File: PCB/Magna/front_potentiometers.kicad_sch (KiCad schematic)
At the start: 24 parts

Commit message: Add final touched to all schematics
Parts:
- removed RV23: 10k, symbol Device:R_Potentiometer_Small
- added RV1421: 10k, symbol Device:R_Potentiometer_Small
- renumbered RV19 to RV1401, RV21 to RV1402, RV24 to RV1403, RV20 to RV1404, RV22 to RV1405, RV18 to RV1406, RV2 to RV1407, RV7 to RV1408, RV11 to RV1409, RV1 to RV1410, RV6 to RV1411, RV10 to RV1412, RV14 to RV1413, RV16 to RV1414, RV13 to RV1415, RV15 to RV1416, RV17 to RV1417, RV9 to RV1418, RV5 to RV1419, RV8 to RV1420, RV3 to RV1422, RV4 to RV1423, RV12 to RV1424
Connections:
- net SPARE7 is gone; now on net SPARE1: RV1403.2
- net GND: now also RV1421.3
- net SPARE1: no longer RV1406.2
- net VDDA: now also RV1421.1
- new net CH1_GAIN: RV1406.2
- new net CH2_GAIN: RV1421.2
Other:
- note added: "GAIN"
- note added: "Spare potentiometers"
- moved on the sheet: RV1401, RV1402, RV1403, RV1404, RV1405, RV1406

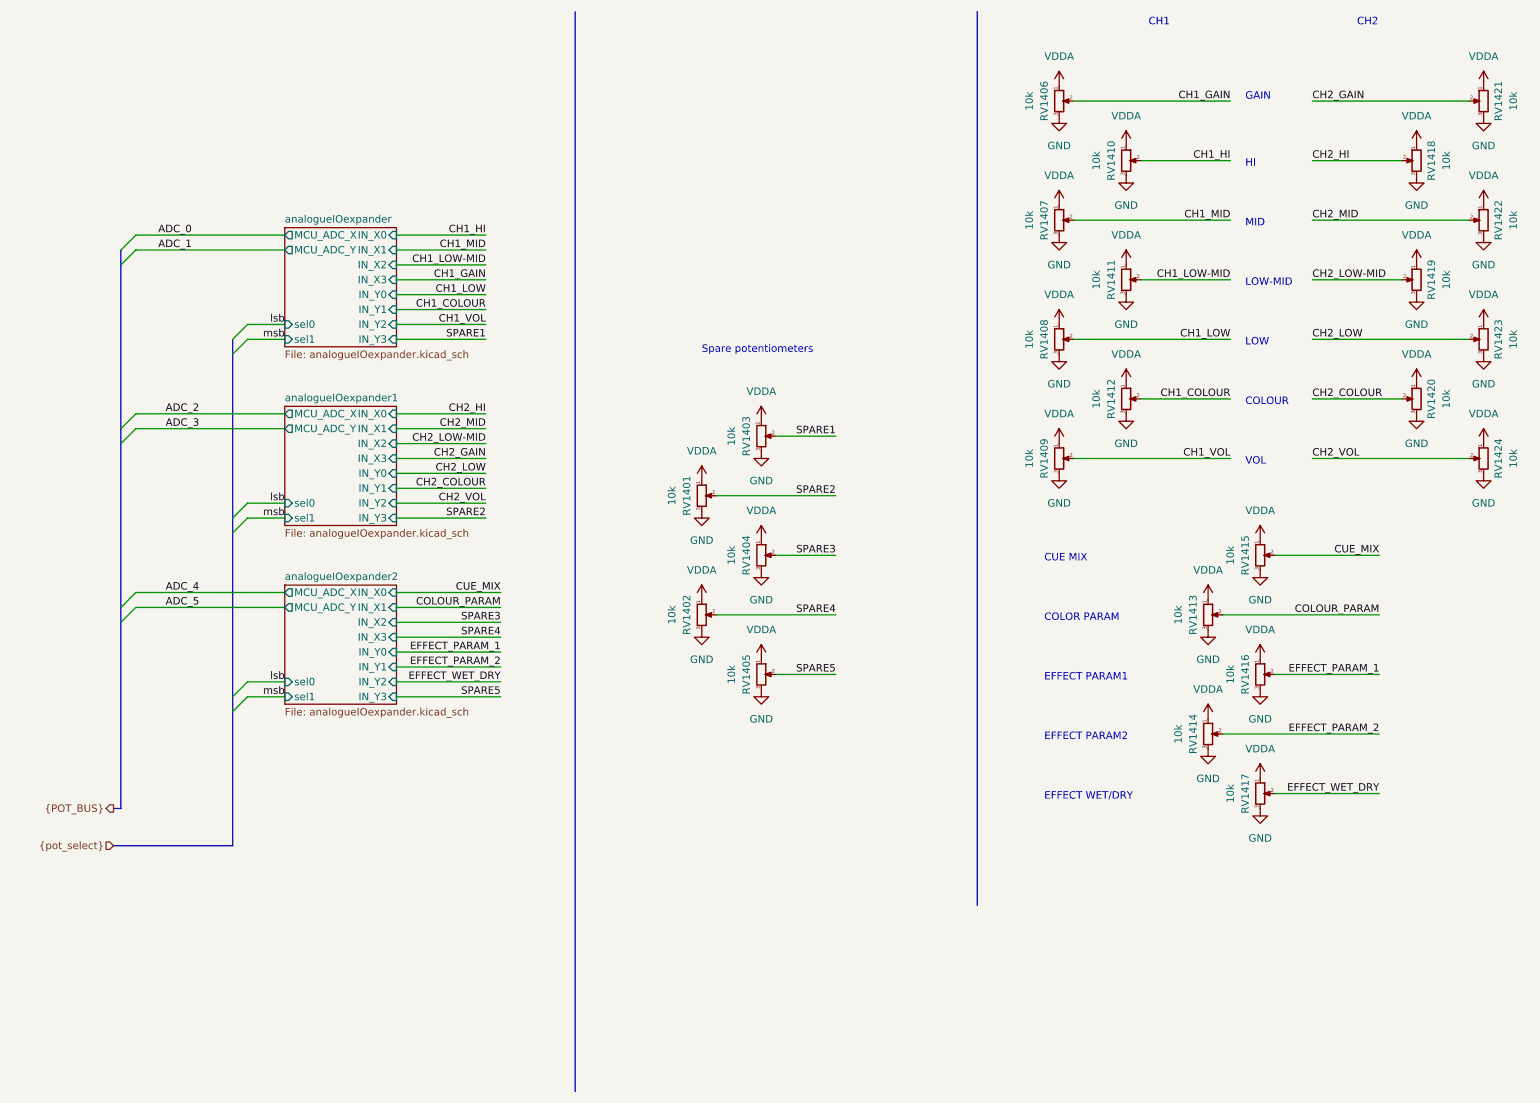
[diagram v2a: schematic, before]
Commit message: Add even more component footprints and partnumbers
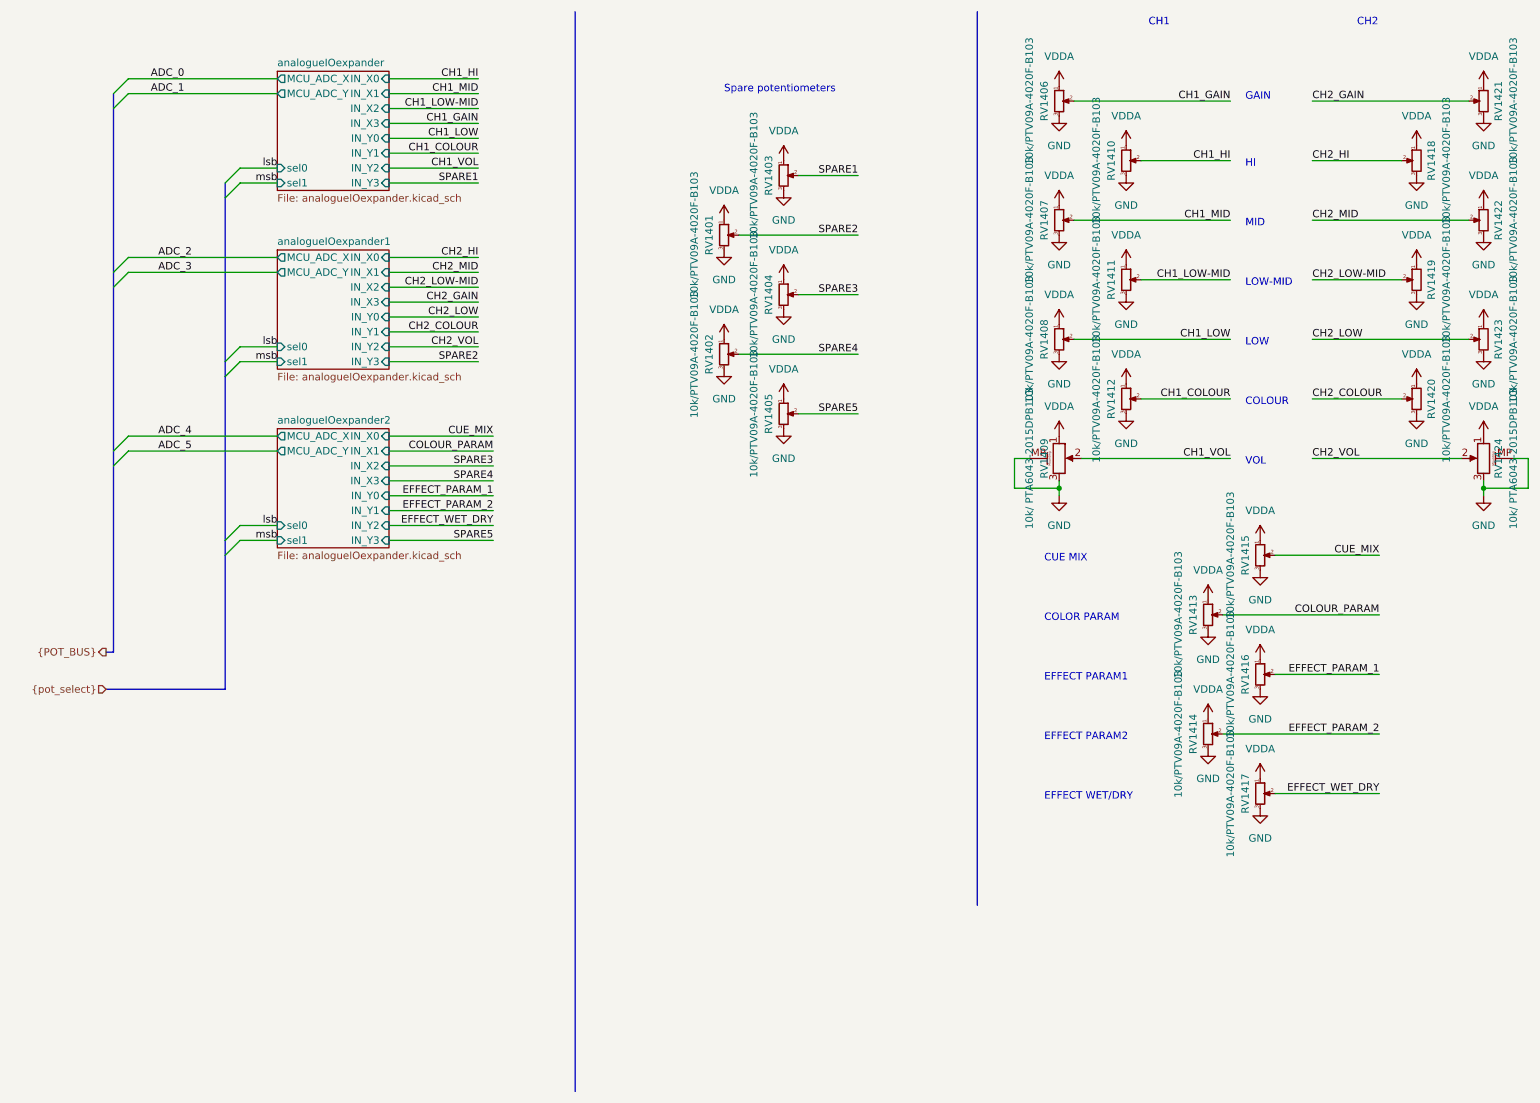
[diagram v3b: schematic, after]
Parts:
- RV1401, RV1402, RV1403, RV1404, RV1405, RV1406, RV1407, RV1408, RV1410, RV1411, RV1412, RV1413, RV1414, RV1415, RV1416, RV1417, RV1418, RV1419, RV1420, RV1421, RV1422, RV1423: value 10k -> 10k/PTV09A-4020F-B103; footprint (none) -> Potentiometer_THT:Potentiometer_Bourns_PTV09A-1_Single_Vertical
- RV1409, RV1424: value 10k -> 10k/ PTA6043-2015DPB103; footprint (none) -> Potentiometer_THT:Potentiometer_Bourns_PTA6043_Single_Slide; symbol Device:R_Potentiometer_Small -> Device:R_Potentiometer_MountingPin
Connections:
- net GND: now also RV1409.MP (MountPin), RV1424.MP (MountPin)
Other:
- moved on the sheet: RV1401, RV1402, RV1403, RV1404, RV1405
